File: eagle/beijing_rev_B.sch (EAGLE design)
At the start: 31 parts, among them IC1 PIC18F2580, IC3 MCP2551SN, IC4 LM2575S, J1 OSTTE-12, J2 A00-108-220-450, Q1 10 MHz

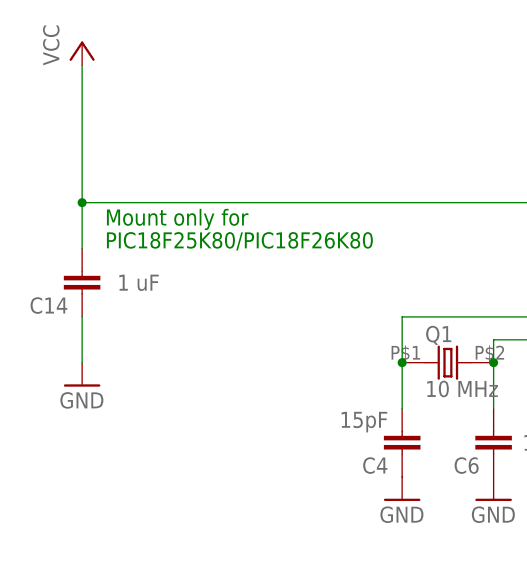
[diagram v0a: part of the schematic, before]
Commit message: Changed value of C14 to 10uF
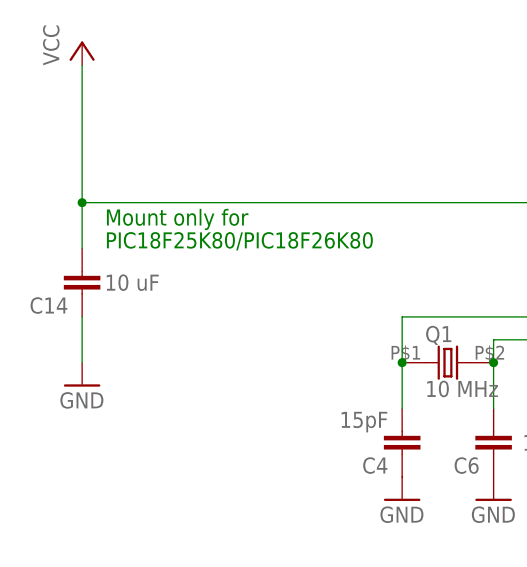
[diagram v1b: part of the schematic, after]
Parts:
- C14: value 1 uF -> 10 uF
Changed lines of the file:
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@@
 <part name="LED2" library="led" deviceset="LED" device="CHIP-LED0805" value="Red LED"/>
 <part name="P+9" library="SUPPLY1" deviceset="VCC" device=""/>
-<part name="C14" library="rcl" deviceset="C-EU" device="C0805" value="1 uF"/>
+<part name="C14" library="rcl" deviceset="C-EU" device="C0805" value="10 uF"/>
 <part name="GND32" library="SUPPLY1" deviceset="GND" device=""/>
 <part name="R17" library="rcl" deviceset="R-EU_" device="R0805" value="120"/>
